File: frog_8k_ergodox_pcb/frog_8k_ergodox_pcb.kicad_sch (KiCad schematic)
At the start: 203 parts, among them J1 USB_C_Receptacle_USB2.0_14P, J2 Conn_01x04_Pin, SW1 SW_DPST_x2, SW2 SW_DPST_x2, U1 PMW3360DM-T2QU, U2 STM32F072CBTx, U3 TLV74318PDBVR, U4 XC6206PxxxMR, U5 SRV05-4

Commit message: Added fuse to vbus.
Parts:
- added F1: Fuse_500mA, Fuse:Fuse_1206_3216Metric_Pad1.42x1.75mm_HandSolder, symbol Device:Fuse_Small
- added H1, H2: MountingHole, MountingHole:MountingHole_2.2mm_M2, symbol Mechanical:MountingHole
- added J10, J3, J4, J5, J6, J7, J8, J9: Conn_01x01_Pin, TestPoint:TestPoint_Pad_1.5x1.5mm, symbol Connector:Conn_01x01_Pin
- J2, U1: now left out of the parts list
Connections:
- net +5V: now also F1.2; no longer J1.A4 (VBUS), J1.A9 (VBUS), J1.B4 (VBUS), J1.B9 (VBUS)
- net ADD7: now reaches U2.11 (PA1)
- net ADD7: now also J10.1 (Pin_1)
- net ADD6: now reaches U2.12 (PA2)
- net ADD6: now also J9.1 (Pin_1)
- net ADD5: now reaches U2.13 (PA3)
- net ADD5: now also J8.1 (Pin_1)
- net ADD4: now reaches U2.29 (PA8)
- net ADD4: now also J7.1 (Pin_1)
- net ADD3: now reaches U2.30 (PA9)
- net ADD3: now also J6.1 (Pin_1)
- net ADD2: now reaches U2.31 (PA10)
- net ADD2: now also J5.1 (Pin_1)
- net ADD1: now reaches U2.34 (PA13)
- net ADD1: now also J4.1 (Pin_1)
- net ADD0: now reaches U2.37 (PA14)
- net ADD0: now also J3.1 (Pin_1)
- new net VBUS: F1.1, J1.A4 (VBUS), J1.A9 (VBUS), J1.B4 (VBUS), J1.B9 (VBUS)
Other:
- note added: "Additional Pins"
- note added: "Boot Switch"
- note added: "Decoupling Capacitors"
- note added: "ESD Protect"
- note added: "JST Connetor"
- note added: "MCU STM32F072CBT6"
- note added: "Regulator TLV74318PDBVR 3.3V-1.8V"
- note added: "Regulator XC6206 5V-3.3V"
- note added: "Reset Switch"
- note added: "SENSOR PMW3360DM-T2QU"
- note added: "Switch Matrix"
- note added: "TrackBall Housing Mounting Hole, M2"
- note added: "USB-C"
- moved on the sheet: J1, R5, R6

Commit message: Added Keyboard Layout on PCB design
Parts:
- J1: footprint Connector_JST:JST_SH_SM04B-SRSS-TB_1x04-1MP_P1.00mm_Horizontal -> Connector_USB:USB_C_Receptacle_HRO_TYPE-C-31-M-12
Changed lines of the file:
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@@
 			)
 		)
-		(property "Footprint" "Connector_JST:JST_SH_SM04B-SRSS-TB_1x04-1MP_P1.00mm_Horizontal"
+		(property "Footprint" "Connector_USB:USB_C_Receptacle_HRO_TYPE-C-31-M-12"
 			(at 346.71 214.63 0)
 			(effects

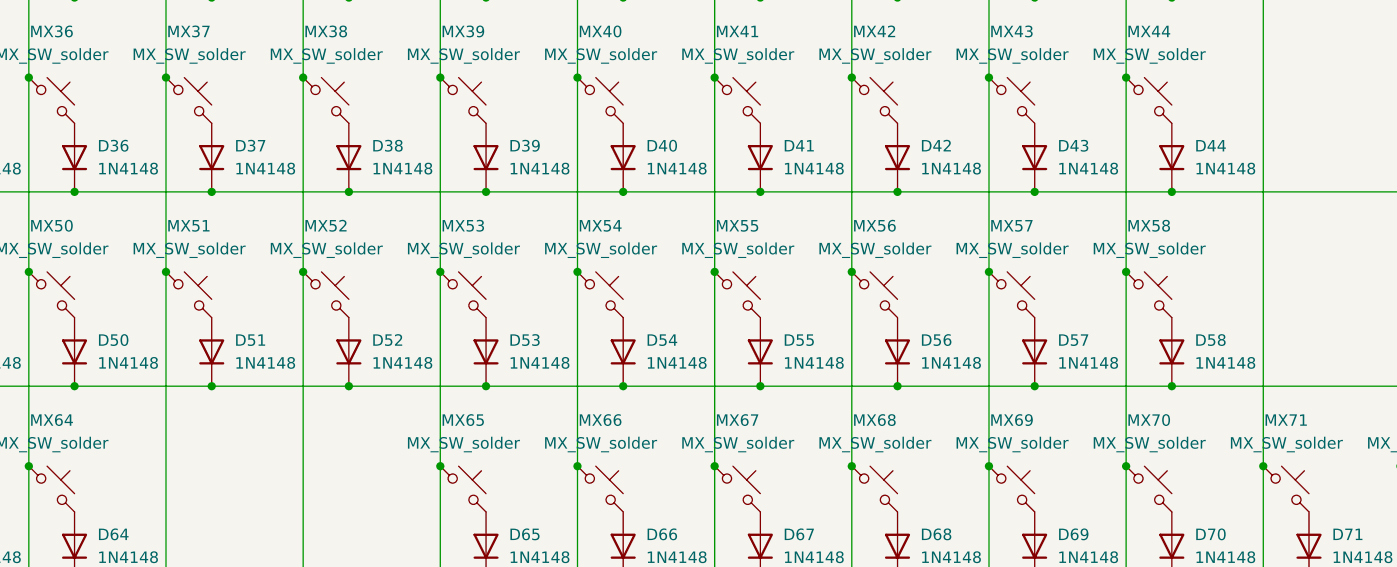
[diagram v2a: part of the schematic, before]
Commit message: Fixed matirix, Reconnect U1 Symbol to Footprint, relocate diode position.
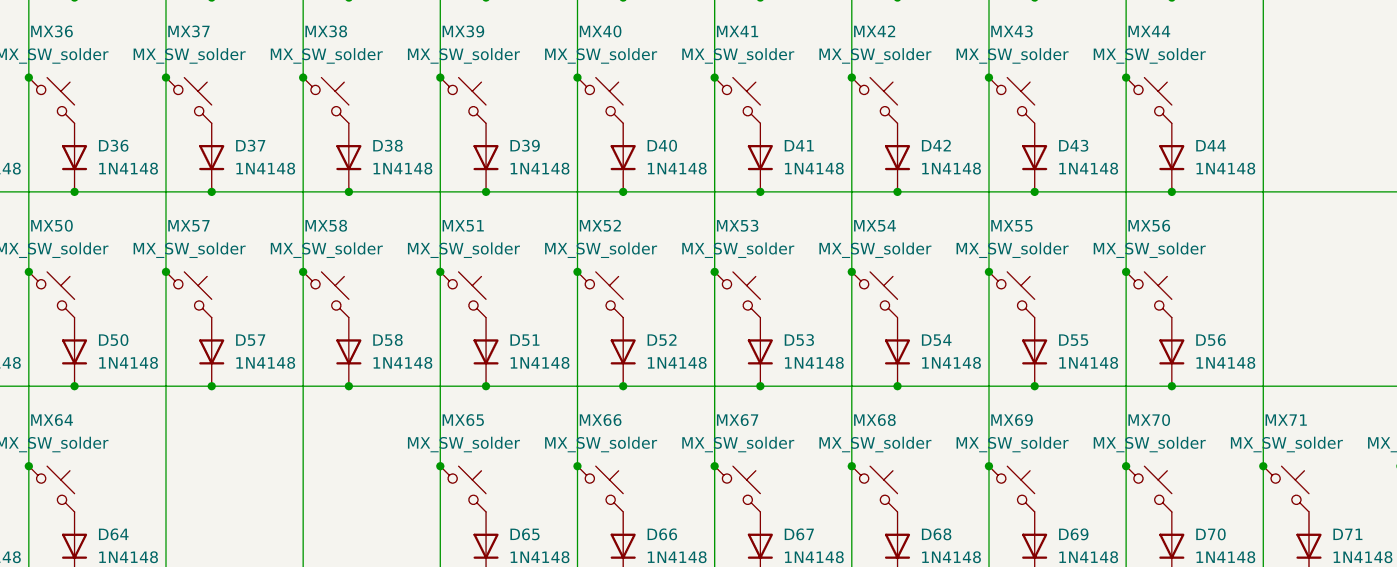
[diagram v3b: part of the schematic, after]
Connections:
- net COL10: now also MX53.1; no longer MX55.1
- net COL11: now also MX54.1; no longer MX56.1
- net COL12: now also MX55.1; no longer MX57.1
- net COL13: now also MX56.1; no longer MX58.1
- net COL6: now also MX57.1; no longer MX51.1
- net COL7: now also MX58.1; no longer MX52.1
- net COL8: now also MX51.1; no longer MX53.1
- net COL9: now also MX52.1; no longer MX54.1
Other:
- moved on the sheet: D51, D52, D53, D54, D55, D56, D57, D58, MX51, MX52, MX53, MX54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

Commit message: Updated PCB design.
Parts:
- removed F1: Fuse_500mA, Fuse:Fuse_1206_3216Metric_Pad1.42x1.75mm_HandSolder, symbol Device:Fuse_Small
- added F1: 500mA, Fuse:Fuse_1206_3216Metric, symbol Device:Polyfuse_Small
- H1: footprint MountingHole:MountingHole_2.2mm_M2 -> MountingHole:MountingHole_2.2mm_M2_ISO14580_Pad
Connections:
- net +5V: now also F1.2
- net VBUS: now also F1.1
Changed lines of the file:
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@@
 	)
 	(symbol
+		(lib_id "Device:Polyfuse_Small")
+		(at 369.57 199.39 90)
+		(unit 1)
+		(exclude_from_sim no)
+		(in_bom yes)
+		(on_board yes)
+		(dnp no)
+		(fields_autoplaced yes)
+		(property "Reference" "F1"
+			(at 369.57 193.04 90)
+			(effects
+				(font
+					(size 1.27 1.27)
+				)
+			)
+		)
+		(property "Value" "500mA"
+			(at 369.57 195.58 90)
+			(effects
+				(font
+					(size 1.27 1.27)
+				)
+			)
+		)
+		(property "Footprint" "Fuse:Fuse_1206_3216Metric"
+			(at 374.65 198.12 0)
+			(effects
+				(font
+					(size 1.27 1.27)
+				)
+				(justify left)
+				(hide yes)
+			)
+		)
+		(property "Datasheet" "~"
+			(at 369.57 199.39 0)
+			(effects
+				(font
+					(size 1.27 1.27)
+				)
+				(hide yes)
+			)
+		)
+		(property "Description" ""
+			(at 369.57 199.39 0)
+			(effects
+				(font
+					(size 1.27 1.27)
+				)
+				(hide yes)
+			)
+		)
+		(property "LCSC" "C70076"
+			(at 369.57 199.39 0)
+			(effects
+				(font
+					(size 1.27 1.27)
+				)
+				(hide yes)
+			)
+		)
+		(pin "1"
+		)
+		(pin "2"
+		)
+		(instances
+			(project "frog_8k_ergodox_pcb"
+				(path "/34ddd234-11af-4a66-9186-ea72bce9a0a9"
+					(reference "F1")
+					(unit 1)
+				)
+			)
+		)
+	)
+	(symbol
 		(lib_id "Device:D")
 		(at 184.15 71.12 90)
@@
 	)
 	(symbol
-		(lib_id "Device:Fuse_Small")
-		(at 369.57 199.39 0)
-		(unit 1)
-		(exclude_from_sim no)
-		(in_bom yes)
-		(on_board yes)
-		(dnp no)
-		(fields_autoplaced yes)
-		(property "Reference" "F1"
-			(at 369.57 194.31 0)
-			(effects
-				(font
-					(size 1.27 1.27)
-				)
-			)
-		)
-		(property "Value" "Fuse_500mA"
-			(at 369.57 196.85 0)
-			(effects
-				(font
-					(size 1.27 1.27)
-				)
-			)
-		)
-		(property "Footprint" "Fuse:Fuse_1206_3216Metric_Pad1.42x1.75mm_HandSolder"
-			(at 369.57 199.39 0)
-			(effects
-				(font
-					(size 1.27 1.27)
-				)
-				(hide yes)
-			)
-		)
-		(property "Datasheet" "~"
-			(at 369.57 199.39 0)
-			(effects
-				(font
-					(size 1.27 1.27)
-				)
-				(hide yes)
-			)
-		)
-		(property "Description" "Fuse, small symbol"
-			(at 369.57 199.39 0)
-			(effects
-				(font
-					(size 1.27 1.27)
-				)
-				(hide yes)
-			)
-		)
-		(pin "1"
-		)
-		(pin "2"
-		)
-		(instances
-			(project ""
-				(path "/34ddd234-11af-4a66-9186-ea72bce9a0a9"
-					(reference "F1")
-					(unit 1)
-				)
-			)
-		)
-	)
-	(symbol
 		(lib_id "Device:D")
 		(at 275.59 157.48 90)
@@
 			)
 		)
-		(property "Footprint" "MountingHole:MountingHole_2.2mm_M2"
+		(property "Footprint" "MountingHole:MountingHole_2.2mm_M2_ISO14580_Pad"
 			(at 331.47 110.49 0)
 			(effects

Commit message: Fixed USB Port 5V to 3.3V, Added Matrix Row/Col
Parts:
- H2: footprint MountingHole:MountingHole_2.2mm_M2 -> MountingHole:MountingHole_2.2mm_M2_ISO7380_Pad
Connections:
- net DN: now also U5.4 (IO3); no longer U5.6 (IO4)
- net DP: now also U5.6 (IO4); no longer U5.3 (IO2)
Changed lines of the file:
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@@
 	)
 	(no_connect
-		(at 180.34 260.35)
+		(at 353.06 151.13)
 	)
 	(no_connect
-		(at 353.06 151.13)
+		(at 180.34 260.35)
 	)
 	(no_connect
@@
 	)
 	(no_connect
-		(at 378.46 151.13)
+		(at 353.06 156.21)
 	)
 	(wire
@@
 		)
 	)
-	(global_label "DP"
-		(shape input)
-		(at 353.06 156.21 180)
-		(fields_autoplaced yes)
-		(effects
-			(font
-				(size 1.27 1.27)
-			)
-			(justify right)
-		)
-		(property "Intersheetrefs" "${INTERSHEET_REFS}"
-			(at 347.5348 156.21 0)
-			(effects
-				(font
-					(size 1.27 1.27)
-				)
-				(justify right)
-				(hide yes)
-			)
-		)
-	)
 	(global_label "COL8"
 		(shape input)
@@
 		)
 	)
-	(global_label "DN"
-		(shape input)
-		(at 378.46 156.21 0)
-		(fields_autoplaced yes)
-		(effects
-			(font
-				(size 1.27 1.27)
-			)
-			(justify left)
-		)
-		(property "Intersheetrefs" "${INTERSHEET_REFS}"
-			(at 384.0457 156.21 0)
-			(effects
-				(font
-					(size 1.27 1.27)
-				)
-				(justify left)
-				(hide yes)
-			)
-		)
-	)
 	(global_label "ROW3"
 		(shape input)
@@
 		)
 	)
+	(global_label "DP"
+		(shape input)
+		(at 378.46 156.21 0)
+		(fields_autoplaced yes)
+		(effects
+			(font
+				(size 1.27 1.27)
+			)
+			(justify left)
+		)
+		(property "Intersheetrefs" "${INTERSHEET_REFS}"
+			(at 383.9852 156.21 0)
+			(effects
+				(font
+					(size 1.27 1.27)
+				)
+				(justify left)
+				(hide yes)
+			)
+		)
+	)
 	(global_label "COL0"
 		(shape input)
@@
 		)
 	)
+	(global_label "DN"
+		(shape input)
+		(at 378.46 151.13 0)
+		(fields_autoplaced yes)
+		(effects
+			(font
+				(size 1.27 1.27)
+			)
+			(justify left)
+		)
+		(property "Intersheetrefs" "${INTERSHEET_REFS}"
+			(at 384.0457 151.13 0)
+			(effects
+				(font
+					(size 1.27 1.27)
+				)
+				(justify left)
+				(hide yes)
+			)
+		)
+	)
 	(global_label "COL5"
 		(shape input)
@@
 			)
 		)
-		(property "Footprint" "MountingHole:MountingHole_2.2mm_M2"
+		(property "Footprint" "MountingHole:MountingHole_2.2mm_M2_ISO7380_Pad"
 			(at 331.47 119.38 0)
 			(effects

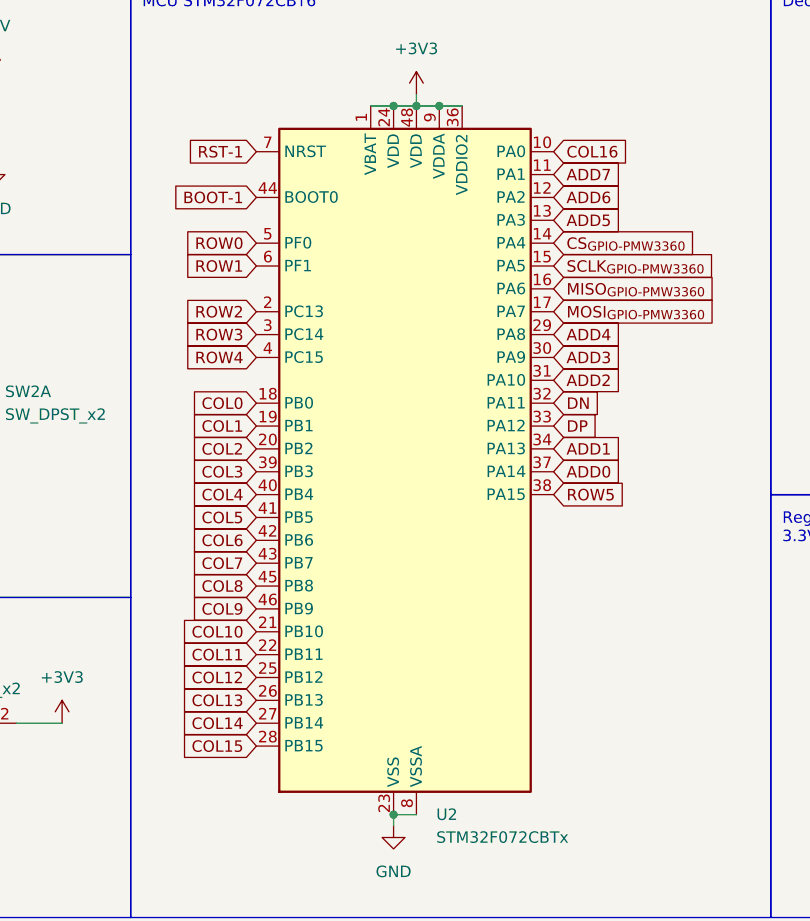
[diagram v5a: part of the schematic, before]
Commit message: Added plate file, Updated Matrix route, Additional Pin routes
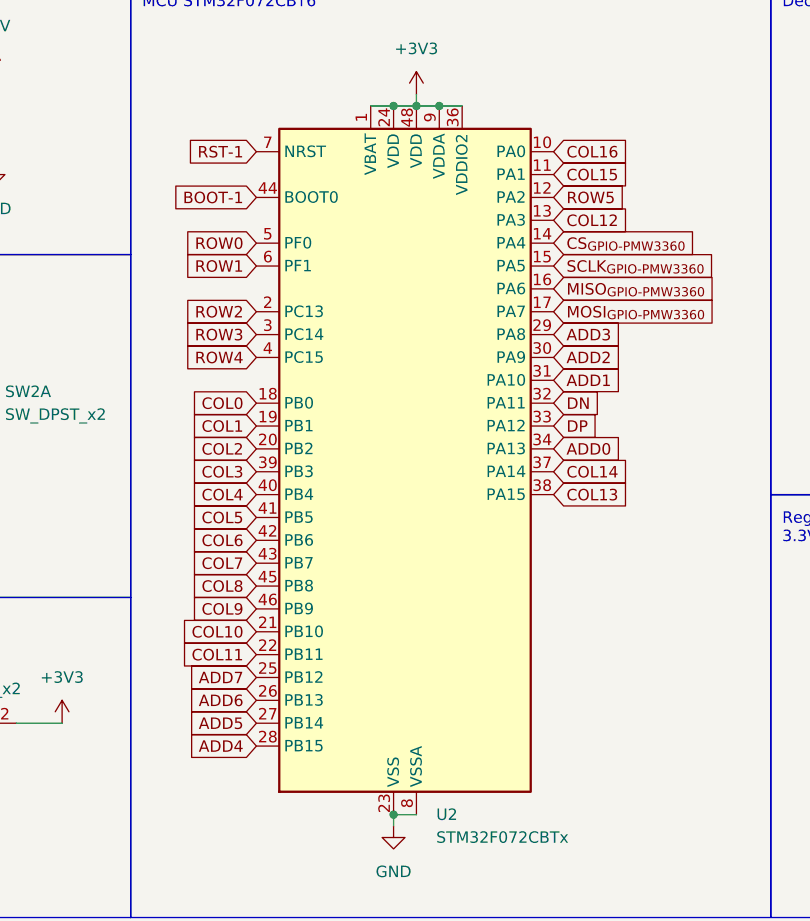
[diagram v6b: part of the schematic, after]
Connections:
- net ADD0: now also U2.34 (PA13); no longer U2.37 (PA14)
- net ADD1: now also U2.31 (PA10); no longer U2.34 (PA13)
- net ADD2: now also U2.30 (PA9); no longer U2.31 (PA10)
- net ADD3: now also U2.29 (PA8); no longer U2.30 (PA9)
- net ADD4: now also U2.28 (PB15); no longer U2.29 (PA8)
- net ADD5: now also U2.27 (PB14); no longer U2.13 (PA3)
- net ADD6: now also U2.26 (PB13); no longer U2.12 (PA2)
- net ADD7: now also U2.25 (PB12); no longer U2.11 (PA1)
- net COL12: now also U2.13 (PA3); no longer U2.25 (PB12)
- net COL13: now also U2.38 (PA15); no longer U2.26 (PB13)
- net COL14: now also U2.37 (PA14); no longer U2.27 (PB14)
- net COL15: now also U2.11 (PA1); no longer U2.28 (PB15)
- net ROW5: now also U2.12 (PA2); no longer U2.38 (PA15)

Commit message: updated footprints...
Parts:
- U1: footprint PMW3360_PCB:16pin‐DIP(PMW3360DM-T2QU) -> pmw3360:PMW3360DM-T2QU 16Pin
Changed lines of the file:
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@@
 			)
 		)
-		(property "Footprint" "PMW3360_PCB:16pin‐DIP(PMW3360DM-T2QU)"
+		(property "Footprint" "pmw3360:PMW3360DM-T2QU 16Pin"
 			(at 257.81 284.48 0)
 			(effects

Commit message: Connect PMW3360 pins.
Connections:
- net V_{IN 3.3V} is gone; now on net +3V3: C3.1, U3.1 (IN), U3.3 (EN)
- net V_{IO VDD~3.3V} is gone; now on net +3V3: R1.1, R2.1, U1.5 (VDDIO)
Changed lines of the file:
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@@
 		)
 	)
-	(global_label "V_{IO VDD~3.3V}"
-		(shape input)
-		(at 283.21 241.3 0)
-		(fields_autoplaced yes)
-		(effects
-			(font
-				(size 1.27 1.27)
-			)
-			(justify left)
-		)
-		(property "Intersheetrefs" "${INTERSHEET_REFS}"
-			(at 296.5754 241.3 0)
-			(effects
-				(font
-					(size 1.27 1.27)
-				)
-				(justify left)
-				(hide yes)
-			)
-		)
-	)
 	(global_label "COL10"
 		(shape input)
@@
 		)
 	)
-	(global_label "V_{IN 3.3V}"
-		(shape input)
-		(at 151.13 257.81 180)
-		(fields_autoplaced yes)
-		(effects
-			(font
-				(size 1.27 1.27)
-			)
-			(justify right)
-		)
-		(property "Intersheetrefs" "${INTERSHEET_REFS}"
-			(at 141.3932 257.81 0)
-			(effects
-				(font
-					(size 1.27 1.27)
-				)
-				(justify right)
-				(hide yes)
-			)
-		)
-	)
 	(global_label "COL9"
 		(shape input)
@@
 		)
 	)
-	(global_label "V_{IO VDD~3.3V}"
-		(shape input)
-		(at 245.11 261.62 180)
-		(fields_autoplaced yes)
-		(effects
-			(font
-				(size 1.27 1.27)
-			)
-			(justify right)
-		)
-		(property "Intersheetrefs" "${INTERSHEET_REFS}"
-			(at 231.7446 261.62 0)
-			(effects
-				(font
-					(size 1.27 1.27)
-				)
-				(justify right)
-				(hide yes)
-			)
-		)
-	)
 	(symbol
 		(lib_id "PCM_marbastlib-mx:MX_SW_solder")
@@
 	)
 	(symbol
+		(lib_id "power:+3V3")
+		(at 245.11 261.62 90)
+		(unit 1)
+		(exclude_from_sim no)
+		(in_bom yes)
+		(on_board yes)
+		(dnp no)
+		(fields_autoplaced yes)
+		(property "Reference" "#PWR025"
+			(at 248.92 261.62 0)
+			(effects
+				(font
+					(size 1.27 1.27)
+				)
+				(hide yes)
+			)
+		)
+		(property "Value" "+3V3"
+			(at 241.3 261.6199 90)
+			(effects
+				(font
+					(size 1.27 1.27)
+				)
+				(justify left)
+			)
+		)
+		(property "Footprint" ""
+			(at 245.11 261.62 0)
+			(effects
+				(font
+					(size 1.27 1.27)
+				)
+				(hide yes)
+			)
+		)
+		(property "Datasheet" ""
+			(at 245.11 261.62 0)
+			(effects
+				(font
+					(size 1.27 1.27)
+				)
+				(hide yes)
+			)
+		)
+		(property "Description" "Power symbol creates a global label with name \"+3V3\""
+			(at 245.11 261.62 0)
+			(effects
+				(font
+					(size 1.27 1.27)
+				)
+				(hide yes)
+			)
+		)
+		(pin "1"
+		)
+		(instances
+			(project "frog_8k_ergodox_pcb"
+				(path "/34ddd234-11af-4a66-9186-ea72bce9a0a9"
+					(reference "#PWR025")
+					(unit 1)
+				)
+			)
+		)
+	)
+	(symbol
 		(lib_id "Device:D")
 		(at 260.35 135.89 90)
@@
 	)
 	(symbol
+		(lib_id "power:+3V3")
+		(at 151.13 257.81 0)
+		(unit 1)
+		(exclude_from_sim no)
+		(in_bom yes)
+		(on_board yes)
+		(dnp no)
+		(fields_autoplaced yes)
+		(property "Reference" "#PWR026"
+			(at 151.13 261.62 0)
+			(effects
+				(font
+					(size 1.27 1.27)
+				)
+				(hide yes)
+			)
+		)
+		(property "Value" "+3V3"
+			(at 151.13 252.73 0)
+			(effects
+				(font
+					(size 1.27 1.27)
+				)
+			)
+		)
+		(property "Footprint" ""
+			(at 151.13 257.81 0)
+			(effects
+				(font
+					(size 1.27 1.27)
+				)
+				(hide yes)
+			)
+		)
+		(property "Datasheet" ""
+			(at 151.13 257.81 0)
+			(effects
+				(font
+					(size 1.27 1.27)
+				)
+				(hide yes)
+			)
+		)
+		(property "Description" "Power symbol creates a global label with name \"+3V3\""
+			(at 151.13 257.81 0)
+			(effects
+				(font
+					(size 1.27 1.27)
+				)
+				(hide yes)
+			)
+		)
+		(pin "1"
+		)
+		(instances
+			(project "frog_8k_ergodox_pcb"
+				(path "/34ddd234-11af-4a66-9186-ea72bce9a0a9"
+					(reference "#PWR026")
+					(unit 1)
+				)
+			)
+		)
+	)
+	(symbol
 		(lib_id "PCM_marbastlib-mx:MX_SW_solder")
 		(at 166.37 107.95 0)
@@
 					(unit 1)
 				)
+			)
+		)
+	)
+	(symbol
+		(lib_id "power:+3V3")
+		(at 283.21 241.3 270)
+		(unit 1)
+		(exclude_from_sim no)
+		(in_bom yes)
+		(on_board yes)
+		(dnp no)
+		(fields_autoplaced yes)
+		(property "Reference" "#PWR024"
+			(at 279.4 241.3 0)
+			(effects
+				(font
+					(size 1.27 1.27)
+				)
+				(hide yes)
+			)
+		)
+		(property "Value" "+3V3"
+			(at 287.02 241.2999 90)
+			(effects
+				(font
+					(size 1.27 1.27)
+				)
+				(justify left)
+			)
+		)
+		(property "Footprint" ""
+			(at 283.21 241.3 0)
+			(effects
+				(font
+					(size 1.27 1.27)
+				)
+				(hide yes)
+			)
+		)
+		(property "Datasheet" ""
+			(at 283.21 241.3 0)
+			(effects
+				(font
+					(size 1.27 1.27)
+				)
+				(hide yes)
+			)
+		)
+		(property "Description" "Power symbol creates a global label with name \"+3V3\""
+			(at 283.21 241.3 0)
+			(effects
+				(font
+					(size 1.27 1.27)
+				)
+				(hide yes)
+			)
+		)
+		(pin "1"
+		)
+		(instances
+			(project "frog_8k_ergodox_pcb"
+				(path "/34ddd234-11af-4a66-9186-ea72bce9a0a9"
+					(reference "#PWR024")
+					(unit 1)
+				)
